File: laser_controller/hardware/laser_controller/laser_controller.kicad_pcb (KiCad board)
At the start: 2 copper layers, 30 x 109 mm, 125 parts, among them J1 AudioJack2_SwitchT, J14 USB_C_Receptacle_USB2.0, J16 SI-46001-F, J2 AudioJack2_SwitchT, J3 AudioJack2_SwitchT, J4 AudioJack2_SwitchT, J5 AudioJack2_SwitchT, J6 Conn_02x05_Odd_Even, SW2 SW_Push, SW3 SW_Push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

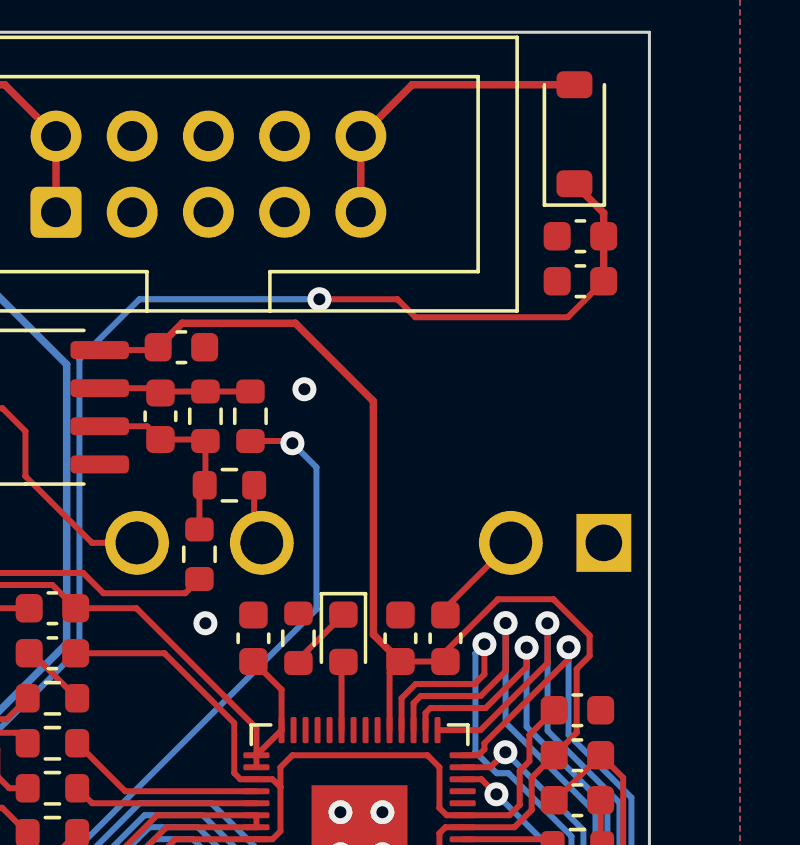
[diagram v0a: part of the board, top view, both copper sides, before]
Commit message: Added electrolytic caps
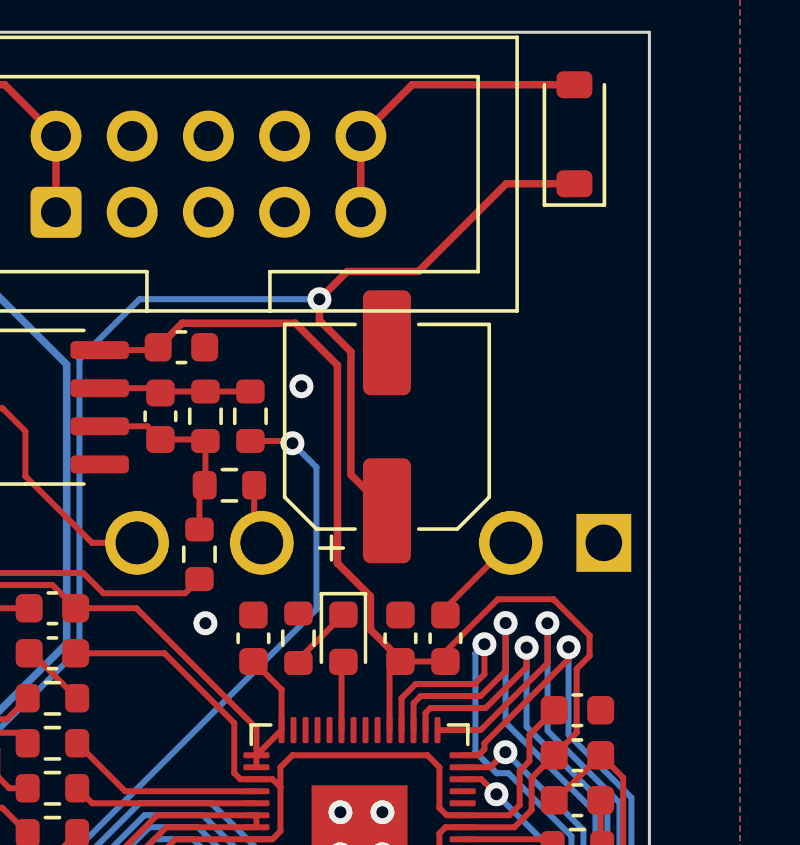
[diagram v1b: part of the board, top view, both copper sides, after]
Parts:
- removed C43, C46: 10u, Capacitor_SMD:C_0603_1608Metric
- added C49: 100u, Capacitor_SMD:CP_Elec_6.3x5.4, F.Cu at (60.0, 65.2)
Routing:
- net +12V: track 185.4 -> 189.6 mm
